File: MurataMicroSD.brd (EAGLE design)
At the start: 92 x 76 mm, 16 parts, among them CON1 CON_TC2030-CTL-NL, IC1 IC_SRAM_23K256_256K_32KBST, U1 IC_BLE_LBCA2HNZYZ-711

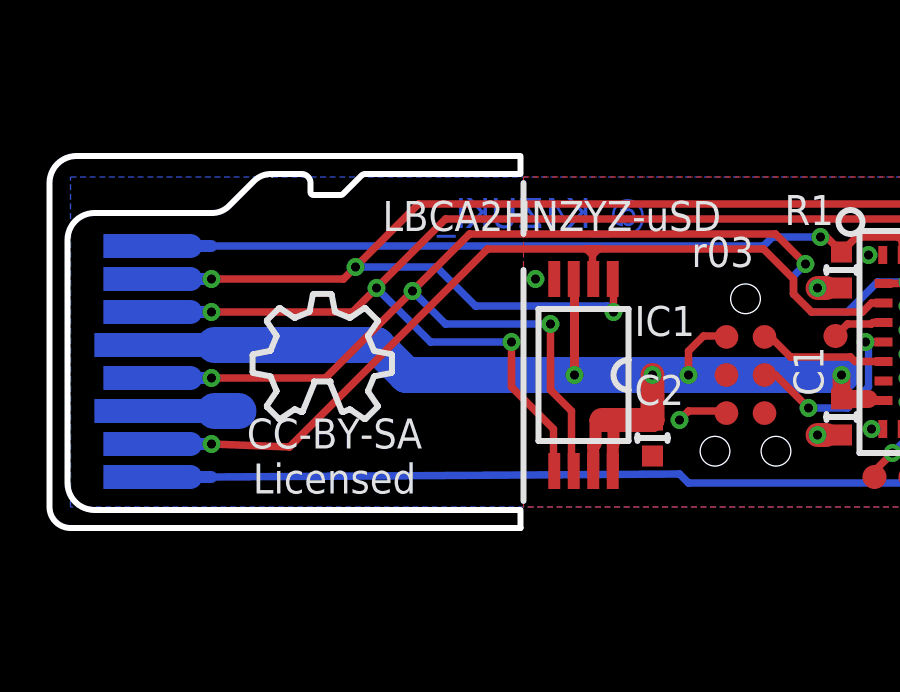
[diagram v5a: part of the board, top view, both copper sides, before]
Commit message: [ uSD ] move silk; tiny trace fix
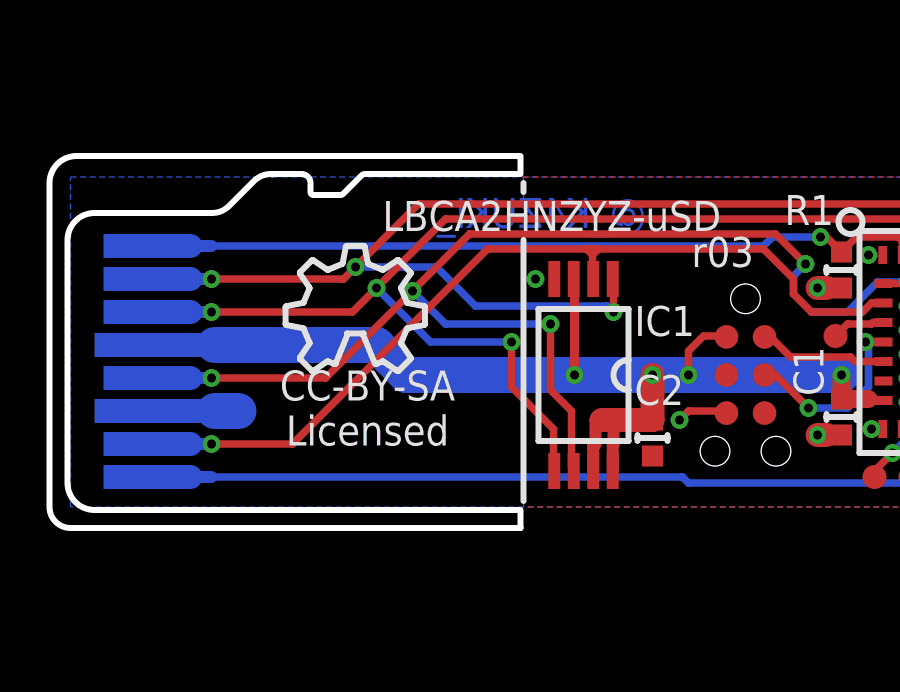
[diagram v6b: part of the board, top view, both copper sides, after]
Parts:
- IC1: value IC_SRAM_23K256_256K_32KBST -> 1265-1139-1-ND

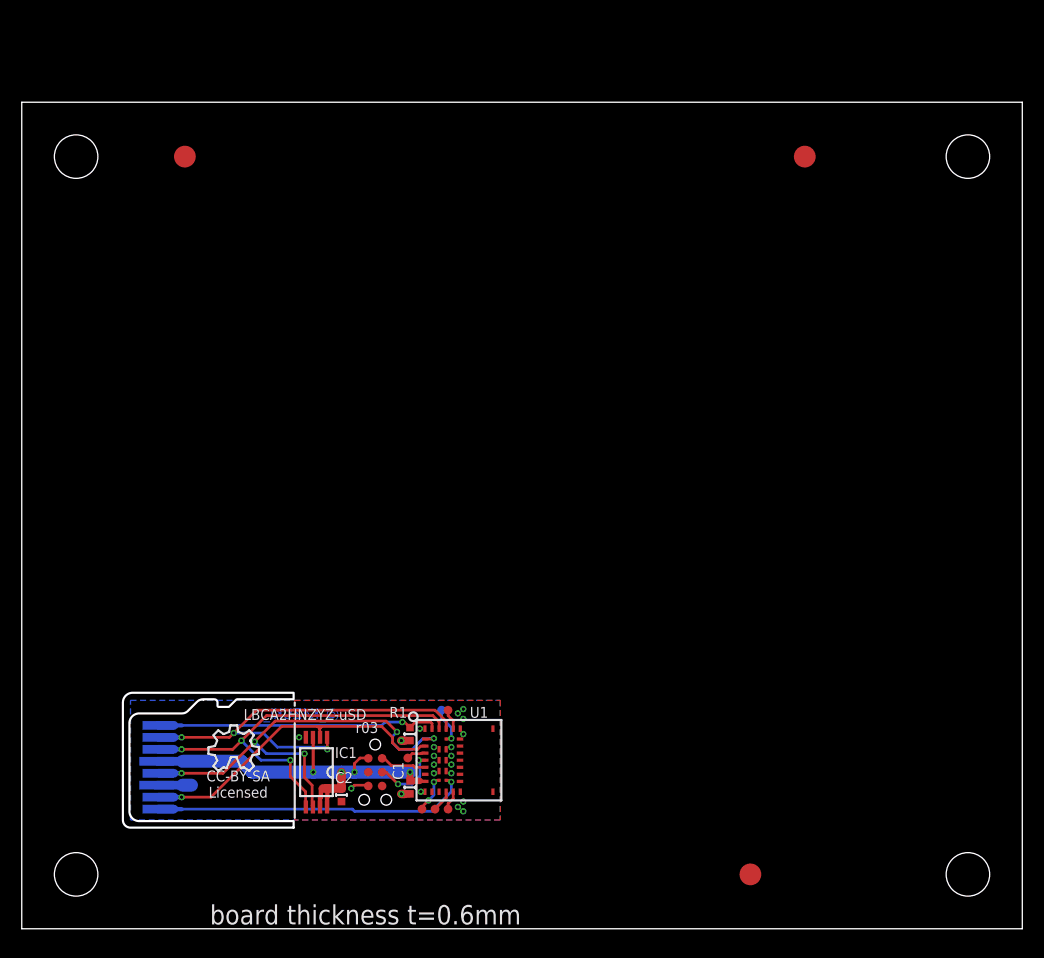
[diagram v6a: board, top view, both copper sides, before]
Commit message: [ uSD ] debug connector moved; increase panel size
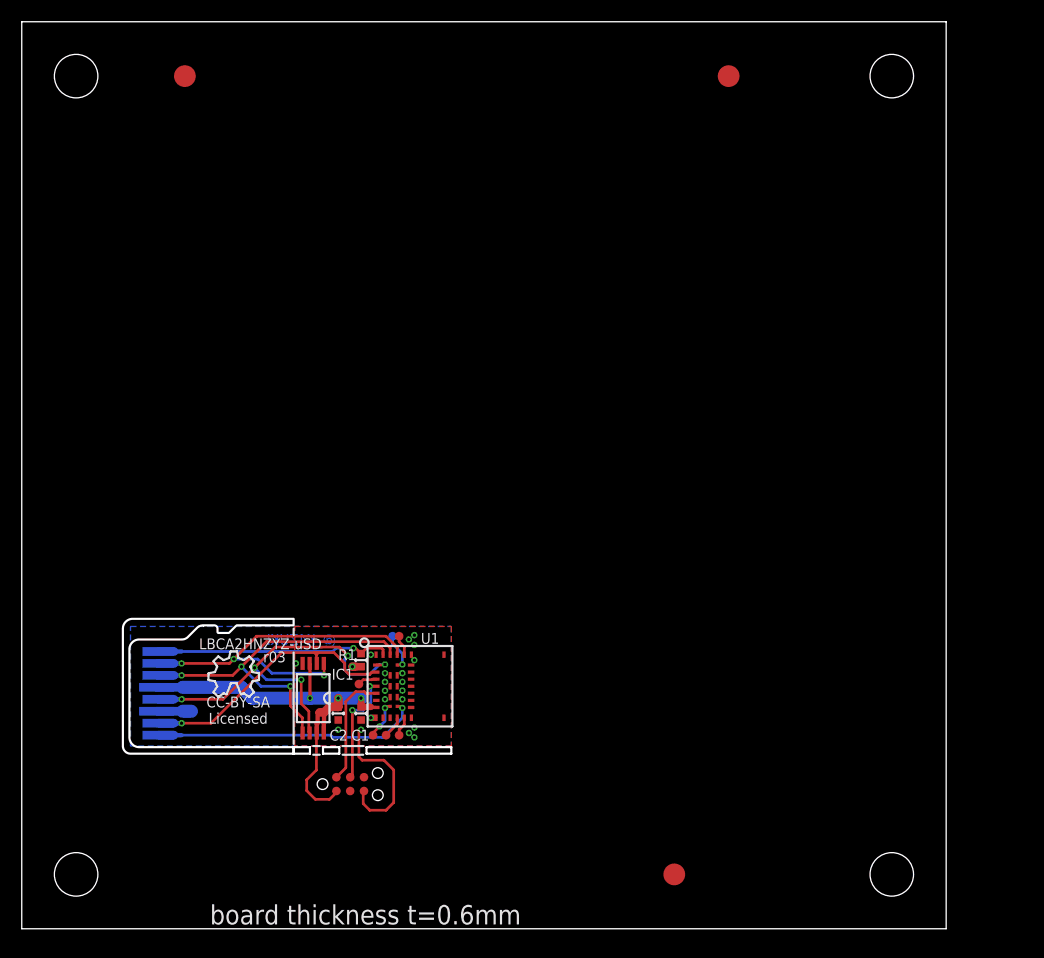
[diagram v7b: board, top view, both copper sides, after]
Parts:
- moved TP102 10.2 mm to (65.0, 78.4)
- moved C1 8.15 mm to (31.2, 19.8)
- moved R1 8.15 mm to (31.2, 24.7)
- moved TP1 8.15 mm to (31.0, 22.5)
- moved TP11 8.15 mm to (32.3, 17.8)
- moved TP7 8.15 mm to (33.5, 17.8)
- moved TP8 8.15 mm to (34.7, 17.8)
- moved U1 8.15 mm to (32.0, 25.8)
- moved TP10 8.15 mm to (34.1, 26.9)
- moved TP9 8.15 mm to (34.7, 26.9)
- moved C2 7.51 mm to (29.1, 19.8)
- moved TP100 7.40 mm to (15.0, 78.4)
- moved TP101 7.00 mm to (60.0, 5.00)
- moved IC1 6.81 mm to (26.8, 21.2)
- moved C100 6.80 mm to (10.0, 27.8)
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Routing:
- net GND: track 6.61 -> 18.2 mm
- net SWDIO: track 4.33 -> 10.6 mm
- net SCK: track 41.1 -> 36.2 mm
- net !CS!: track 38.9 -> 34.1 mm
- net VPP: track 29.4 -> 24.7 mm
- net RXD_MOSI: track 38.1 -> 33.5 mm
- net MISO: track 30.1 -> 25.6 mm
- net N$1: track 26.2 -> 21.7 mm
- net SWCLK: track 6.39 -> 10.4 mm
- net 3.3V: track 38.3 -> 40.5 mm, vias 4 -> 3
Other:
- board size 92 x 76 mm -> 85 x 83.4 mm

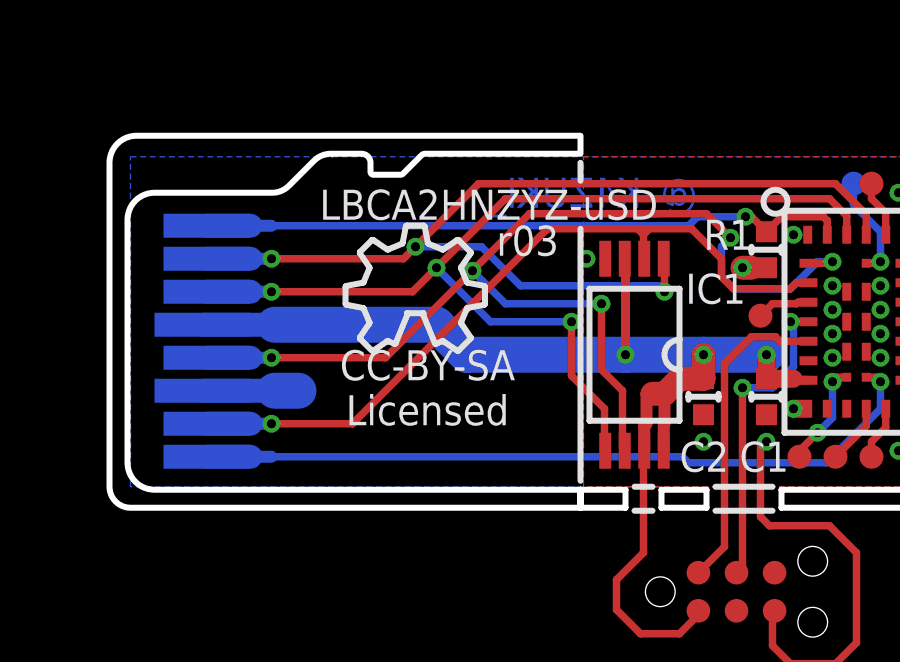
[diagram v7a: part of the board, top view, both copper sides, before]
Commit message: [ uSD ] OSHW icon replaced from library
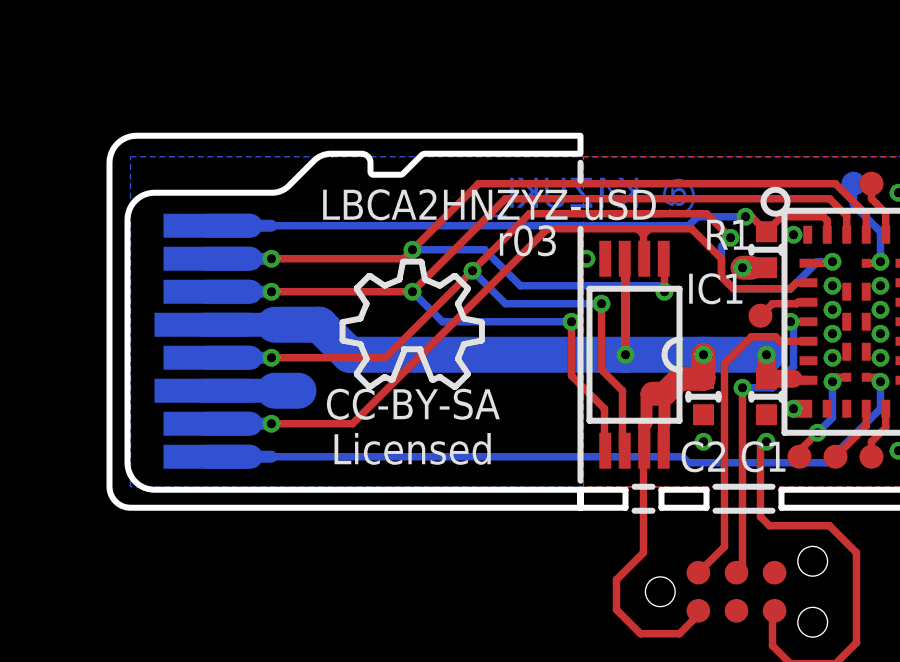
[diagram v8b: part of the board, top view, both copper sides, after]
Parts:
- added U$1: ICON_OSHW, mylib:ICON_OSHW
